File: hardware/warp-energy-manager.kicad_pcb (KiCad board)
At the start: 4 copper layers, 68 x 87 mm, 90 parts, among them J101 Boot, P101 CON-SENSOR2, P102 Relay, P103 L+N, P104 OUT, P105 INPUT, P106 DNP, P110 MODBUS, P111 Debug, Q102 SI2305CDS-T1-GE3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

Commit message: generate production version
 add fiducials
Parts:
- added Fiducial_Mark: VAL**, kicad-libraries:Fiducial_Mark, F.Cu at (97.3, 53.5)
- added Fiducial_Mark: VAL**, kicad-libraries:Fiducial_Mark, F.Cu at (95.3, 135.6)
- added Fiducial_Mark: VAL**, kicad-libraries:Fiducial_Mark, F.Cu at (158.3, 128.6)
- added Fiducial_Mark: VAL**, kicad-libraries:Fiducial_Mark, F.Cu at (157.3, 54.5)
- added G***: LOGO, kicad-libraries:Logo_31x31, F.Cu at (101.0, 105.3)
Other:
- board text added: "12V"
- board text added: "5V"
- board text added: "Copyright Tinkerforge GmbH 2022. This documentation describes Open Hardware and is licensed under the CERN OHL v. 1.1. You may redistribute and modify this documentation under the terms of the CERN OHL v.1.1. (http://ohwr.org/cernohl). This documentation is distributed WITHOUT ANY EXPRESS OR IMPLIED WARRANTY, INCLUDING OF MERCHANTABILITY, SATISFACTORY QUALITY AND FITNESS FOR A PARTICULAR PURPOSE.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"
- board text added: "GND"
- board text removed: "Copyright Tinkerforge GmbH 2021. This documentation describes Open Hardware and is licensed under the CERN OHL v. 1.1. You may redistribute and modify this documentation under the terms of the CERN OHL v.1.1. (http://ohwr.org/cernohl). This documentation is distributed WITHOUT ANY EXPRESS OR IMPLIED WARRANTY, INCLUDING OF MERCHANTABILITY, SATISFACTORY QUALITY AND FITNESS FOR A PARTICULAR PURPOSE.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"
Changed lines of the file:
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@@
   (general
     (thickness 1.6)
-    (drawings 34)
+    (drawings 37)
     (tracks 801)
     (zones 0)
-    (modules 90)
+    (modules 95)
     (nets 102)
   )
@@
   (title_block
     (title "Energy Manager Bricklet")
-    (date 2021-12-16)
+    (date 2022-01-18)
     (rev 1.3)
     (company "Tinkerforge GmbH")
     (comment 1 "Licensed under CERN OHL v.1.1")
-    (comment 2 "Copyright (©) 2021, B.Nordmeyer <bastian@tinkerforge.com>")
+    (comment 2 "Copyright (©) 2022, B.Nordmeyer <bastian@tinkerforge.com>")
   )
   (layers
@@
     (add_net VCC)
   )
+  (module kicad-libraries:Logo_31x31 (layer F.Cu)
+    (at 100.95 105.35 180)
+    (fp_text reference G*** (at 0 0) (layer F.SilkS) hide
+      (effects (font (size 0.1 0.1) (thickness 0.025)))
+    )
+    (fp_text value LOGO (at 0.75 0) (layer F.SilkS) hide
+      (effects (font (size 0.1 0.1) (thickness 0.025)))
+    )
+    (fp_poly (pts (xy 0.483809 -0.030238) (xy 1.016 -0.030238) (xy 1.016 0.27819) (xy 0.483809 0.27819)
+      (xy 0.483809 1.016) (xy 0.145142 1.016) (xy 0.145142 -0.459619) (xy 0.483809 -0.459619)
+      (xy 0.483809 -0.030238)) (layer F.SilkS) (width 0.01))
+    (fp_poly (pts (xy 1.016 -0.701524) (xy -0.090715 -0.701524) (xy -0.090715 1.016) (xy -0.429381 1.016)
+      (xy -0.429381 -0.701524) (xy -1.028096 -0.701524) (xy -1.028096 -1.034143) (xy 1.016 -1.034143)
+      (xy 1.016 -0.701524)) (layer F.SilkS) (width 0.01))
+    (fp_poly (pts (xy 1.614714 1.221619) (xy 1.427238 1.221619) (xy 1.427238 -1.439334) (xy -1.62681 -1.439334)
+      (xy -1.62681 -1.62681) (xy 1.614714 -1.62681) (xy 1.614714 1.221619)) (layer F.SilkS) (width 0.01))
+    (fp_poly (pts (xy -1.433286 1.42119) (xy 1.614714 1.42119) (xy 1.614714 1.608666) (xy -1.62681 1.608666)
+      (xy -1.62681 -1.239762) (xy -1.433286 -1.239762) (xy -1.433286 1.42119)) (layer F.SilkS) (width 0.01))
+  )
+  (module kicad-libraries:Fiducial_Mark (layer F.Cu)
+    (at 97.35 53.55)
+    (attr smd)
+    (fp_text reference Fiducial_Mark (at 0 0) (layer F.SilkS) hide
+      (effects (font (size 0.127 0.127) (thickness 0.03302)))
+    )
+    (fp_text value VAL** (at 0 -0.29972) (layer F.SilkS) hide
+      (effects (font (size 0.127 0.127) (thickness 0.03302)))
+    )
+    (fp_circle (center 0 0) (end 1.15062 0) (layer Dwgs.User) (width 0.01016))
+    (pad 1 smd circle (at 0 0) (size 1.00076 1.00076) (layers F.Cu F.Paste F.Mask)
+      (clearance 0.65024))
+  )
+  (module kicad-libraries:Fiducial_Mark (layer F.Cu)
+    (at 95.35 135.55)
+    (attr smd)
+    (fp_text reference Fiducial_Mark (at 0 0) (layer F.SilkS) hide
+      (effects (font (size 0.127 0.127) (thickness 0.03302)))
+    )
+    (fp_text value VAL** (at 0 -0.29972) (layer F.SilkS) hide
+      (effects (font (size 0.127 0.127) (thickness 0.03302)))
+    )
+    (fp_circle (center 0 0) (end 1.15062 0) (layer Dwgs.User) (width 0.01016))
+    (pad 1 smd circle (at 0 0) (size 1.00076 1.00076) (layers F.Cu F.Paste F.Mask)
+      (clearance 0.65024))
+  )
+  (module kicad-libraries:Fiducial_Mark (layer F.Cu)
+    (at 158.35 128.55)
+    (attr smd)
+    (fp_text reference Fiducial_Mark (at 0 0) (layer F.SilkS) hide
+      (effects (font (size 0.127 0.127) (thickness 0.03302)))
+    )
+    (fp_text value VAL** (at 0 -0.29972) (layer F.SilkS) hide
+      (effects (font (size 0.127 0.127) (thickness 0.03302)))
+    )
+    (fp_circle (center 0 0) (end 1.15062 0) (layer Dwgs.User) (width 0.01016))
+    (pad 1 smd circle (at 0 0) (size 1.00076 1.00076) (layers F.Cu F.Paste F.Mask)
+      (clearance 0.65024))
+  )
+  (module kicad-libraries:Fiducial_Mark (layer F.Cu)
+    (at 157.35 54.55)
+    (attr smd)
+    (fp_text reference Fiducial_Mark (at 0 0) (layer F.SilkS) hide
+      (effects (font (size 0.127 0.127) (thickness 0.03302)))
+    )
+    (fp_text value VAL** (at 0 -0.29972) (layer F.SilkS) hide
+      (effects (font (size 0.127 0.127) (thickness 0.03302)))
+    )
+    (fp_circle (center 0 0) (end 1.15062 0) (layer Dwgs.User) (width 0.01016))
+    (pad 1 smd circle (at 0 0) (size 1.00076 1.00076) (layers F.Cu F.Paste F.Mask)
+      (clearance 0.65024))
+  )
   (module kicad-libraries:C0603F (layer F.Cu)
     (at 144.25 84.85)
@@
     )
   )
+  (gr_text 5V (at 158.75 125.55 180) (layer F.SilkS)
+    (effects (font (size 0.7 0.7) (thickness 0.15)) (justify left))
+  )
+  (gr_text GND (at 158.75 123.55 180) (layer F.SilkS)
+    (effects (font (size 0.7 0.7) (thickness 0.15)) (justify left))
+  )
+  (gr_text 12V (at 158.75 121.55 180) (layer F.SilkS)
+    (effects (font (size 0.7 0.7) (thickness 0.15)) (justify left))
+  )
   (gr_text "Fuse Relay" (at 109.55 93.65 180) (layer F.SilkS)
     (effects (font (size 0.7 0.7) (thickness 0.15)))
@@
     (effects (font (size 0.7 0.7) (thickness 0.15)))
   )
-  (gr_text "R1 R2" (at 138.2 60.55 180) (layer F.SilkS)
+  (gr_text "R1 R2" (at 138.25 60.55 180) (layer F.SilkS)
     (effects (font (size 0.7 0.7) (thickness 0.15)))
   )
@@
   (gr_line (start 160.35 51.55) (end 160.35 138.55) (layer Edge.Cuts) (width 0.09906))
   (gr_line (start 92.35 51.55) (end 160.35 51.55) (layer Edge.Cuts) (width 0.09906))
-  (gr_text "Copyright Tinkerforge GmbH 2021.\nThis documentation describes Open Hardware and is licensed under the\nCERN OHL v. 1.1.\nYou may redistribute and modify this documentation under the terms of the\nCERN OHL v.1.1. (http://ohwr.org/cernohl). This documentation is distributed\nWITHOUT ANY EXPRESS OR IMPLIED WARRANTY, INCLUDING OF\nMERCHANTABILITY, SATISFACTORY QUALITY AND FITNESS FOR A\nPARTICULAR PURPOSE. Please see the CERN OHL v.1.1 for applicable\nconditions" (at 147.85 182.35) (layer Cmts.User)
+  (gr_text "Copyright Tinkerforge GmbH 2022.\nThis documentation describes Open Hardware and is licensed under the\nCERN OHL v. 1.1.\nYou may redistribute and modify this documentation under the terms of the\nCERN OHL v.1.1. (http://ohwr.org/cernohl). This documentation is distributed\nWITHOUT ANY EXPRESS OR IMPLIED WARRANTY, INCLUDING OF\nMERCHANTABILITY, SATISFACTORY QUALITY AND FITNESS FOR A\nPARTICULAR PURPOSE. Please see the CERN OHL v.1.1 for applicable\nconditions" (at 147.85 182.35) (layer Cmts.User)
     (effects (font (size 0.8 0.8) (thickness 0.15)))
   )

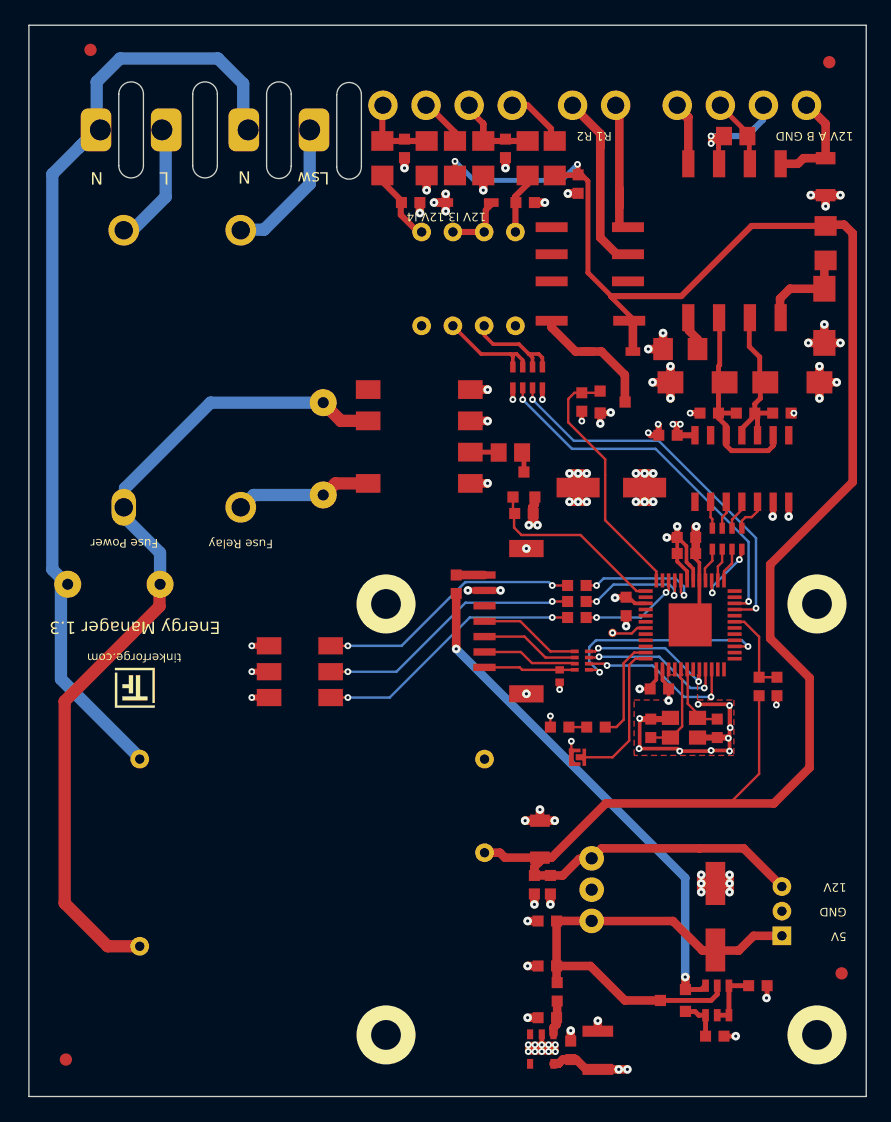
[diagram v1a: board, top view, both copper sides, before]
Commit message: add version 1.4
 add micro sd card socket
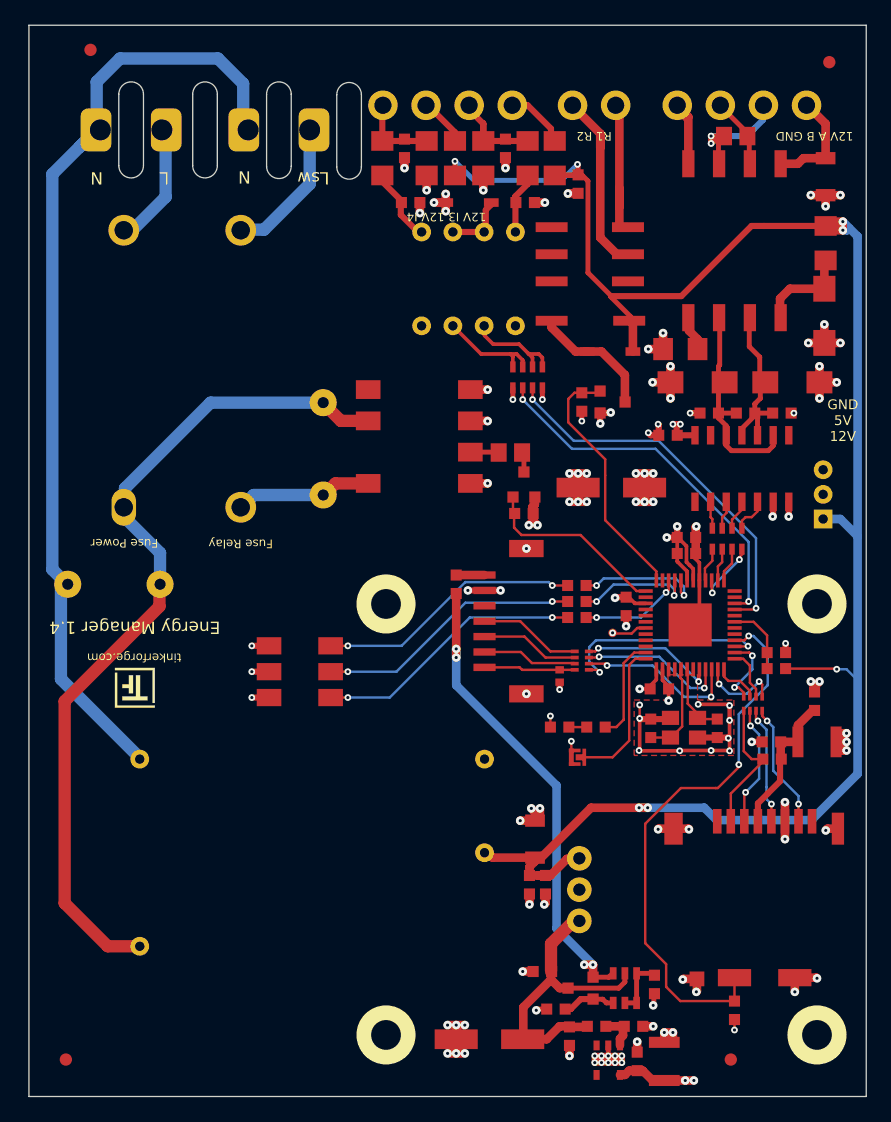
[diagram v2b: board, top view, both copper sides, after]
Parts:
- added C116: 100uF, kicad-libraries:C1210, F.Cu at (156.3, 109.8)
- added C117: 100nF, C0603F, F.Cu at (152.7, 109.8)
- added J102: DM3CS, kicad-libraries:SD-Card-DM3CS, F.Cu at (151.2, 122.5)
- added L102: FB, kicad-libraries:R0603F, F.Cu at (156.2, 106.5)
- added R106: 10k, kicad-libraries:R0603F, F.Cu at (149.7, 131.6)
- added R109: 10k, kicad-libraries:R0603F, F.Cu at (152.7, 111.2)
- added RP103: 82, kicad-libraries:4X0402, F.Cu at (151.2, 106.7)
- moved P106 34.0 mm to (156.8, 89.7)
- moved C108 20.9 mm to (129.8, 133.9), turned to 0 degrees
- moved R133 13.1 mm to (135.2, 131.4), turned to 0 degrees
- moved Fiducial_Mark 11.4 mm to (149.3, 135.6)
- moved R140 8.40 mm to (143.2, 129.4), turned to 90 degrees
- moved Q105 7.57 mm to (137.2, 129.8)
- moved U103 7.57 mm to (140.8, 129.8)
- moved C106 7.03 mm to (141.4, 132.8), turned to 0 degrees
- moved C103 5.98 mm to (136.2, 133.7), turned to 270 degrees
- moved U110 5.47 mm to (139.4, 135.6)
- moved C110 5.47 mm to (141.8, 135.7)
- moved C111 5.47 mm to (143.9, 135.7)
- moved L101 4.25 mm to (138.4, 132.8), turned to 180 degrees
- moved C126 4.12 mm to (134.1, 128.4)
- moved R108 2.75 mm to (153.1, 102.5), turned to 180 degrees
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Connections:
- P106 pad 1: 5V -> VCC
- P106 pad 2: GND -> 5V
- P106 pad 3: VCC -> GND
- U101 pad 1: Net-(U101-Pad1) -> SD-CLK
- U101 pad 2: Net-(U101-Pad2) -> SD-CS
- U101 pad 4: Net-(U101-Pad4) -> SD-CDS
- U101 pad 47: Net-(U101-Pad47) -> SD-MISO
- U101 pad 48: Net-(U101-Pad48) -> SD-MOSI
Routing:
- net SD-CDS: track 0.00 -> 45.2 mm, vias 0 -> 2
- net 5V: track 40.0 -> 81.3 mm
- net GND: track 112.8 -> 132.5 mm, vias 88 -> 103
- net VCC: track 166.6 -> 154.6 mm, vias 2 -> 7
- net Net-(C116-Pad1): track 0.00 -> 11.6 mm
- net Net-(J102-Pad2): track 0.00 -> 11.2 mm
- net Net-(J102-Pad7): track 0.00 -> 10.1 mm, vias 0 -> 2
- net Net-(J102-Pad3): track 0.00 -> 9.78 mm, vias 0 -> 2
- net Net-(J102-Pad5): track 0.00 -> 9.51 mm, vias 0 -> 2
- net SD-MISO: track 0.00 -> 6.51 mm, vias 0 -> 2
- net SD-CS: track 0.00 -> 5.93 mm, vias 0 -> 2
- net SD-CLK: track 0.00 -> 4.21 mm
- net SD-MOSI: track 0.00 -> 3.65 mm
- net 3V3: track 71.5 -> 74.3 mm, vias 23 -> 26
- net Net-(L103-Pad1): track 41.4 -> 39.4 mm, vias 2 -> 4
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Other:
- board text added: "Energy Manager 1.4"
- board text added: "GND 5V 12V"
- board text removed: "12V"
- board text removed: "5V"
- board text removed: "Energy Manager 1.3"
- board text removed: "GND"

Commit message: add 32.768kHz crystal for rtc
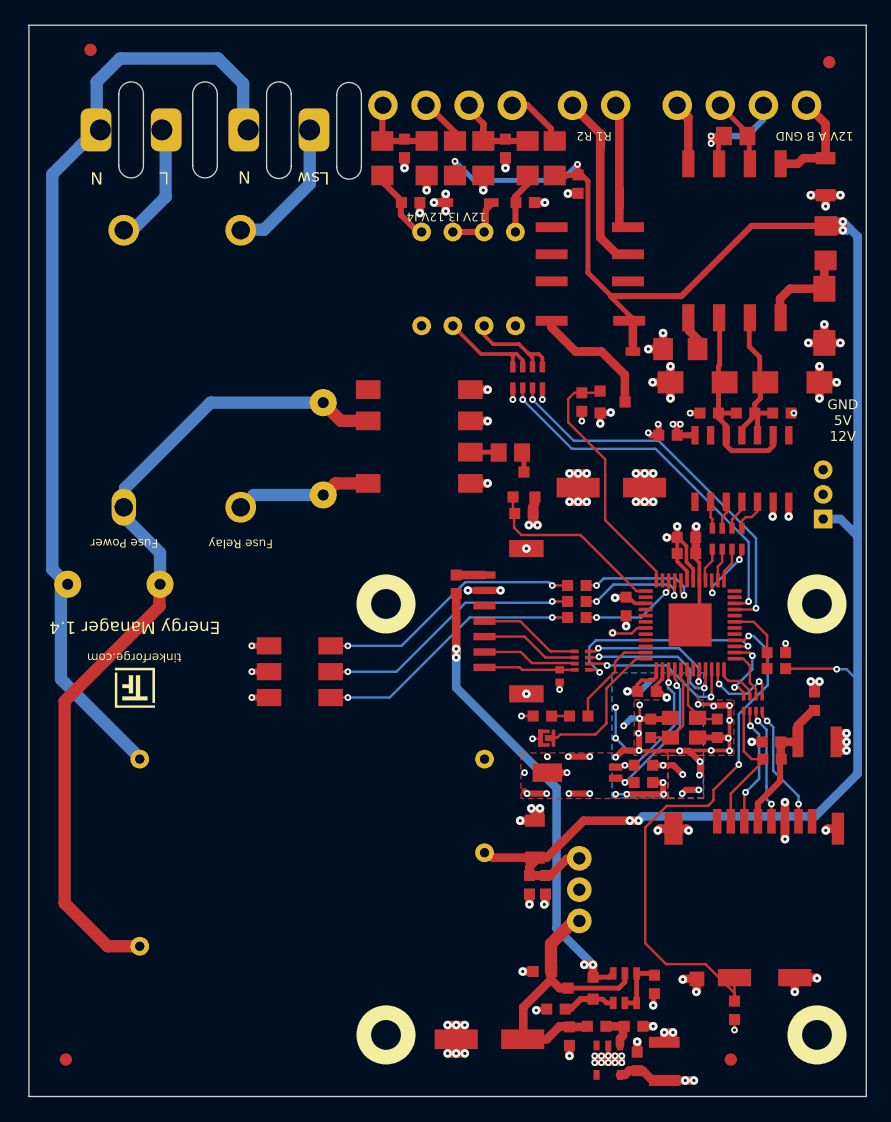
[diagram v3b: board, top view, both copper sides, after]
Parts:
- added C118: 10pF, C0603F, F.Cu at (142.2, 113.0)
- added C119: 10pF, C0603F, F.Cu at (142.2, 111.7)
- added X102: 32.768kHz, kicad-libraries:AB26TRQ, F.Cu at (134.4, 112.2)
- moved J101 2.94 mm to (134.4, 109.5)
- moved R124 1.66 mm to (137.0, 107.7)
- moved D103 1.66 mm to (134.1, 107.7)
- moved C102 1.02 mm to (142.6, 105.7)
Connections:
- U101 pad 39: Net-(U101-Pad39) -> RTC-XTAL1
- U101 pad 40: Net-(U101-Pad40) -> RTC-XTAL2
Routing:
- net GND: track 132.5 -> 171.3 mm, vias 103 -> 128
- net RTC-XTAL2: track 0.00 -> 12.9 mm, vias 0 -> 2
- net RTC-XTAL1: track 0.00 -> 11.7 mm, vias 0 -> 2
- net VCC: track 154.6 -> 153.1 mm
- net S-CS: track 11.2 -> 11.8 mm
- net S-CLK: track 12.0 -> 12.7 mm
- net SD-CDS: track 45.2 -> 44.7 mm
- added copper zone on B.Cu, net GND

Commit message: specify rtc capacitors
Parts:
- C118, C119: value 10pF -> 15pF
